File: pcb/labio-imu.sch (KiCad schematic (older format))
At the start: 33 parts, among them SW501 DIP_SWITCH_X04, U501 LSM303D, U502 BMP280, U503 L3GD20H

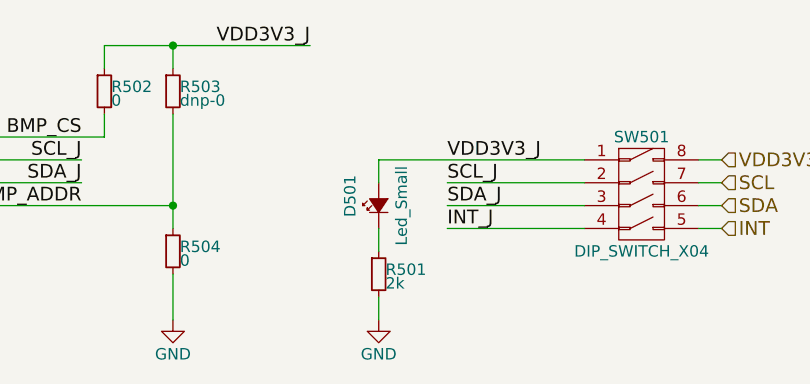
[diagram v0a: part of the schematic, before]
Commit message: add bom. change led resistors to 220 and dnp rpi hat eeprom
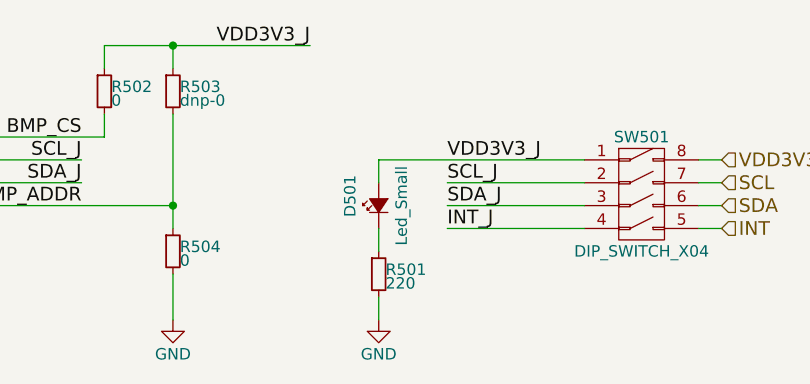
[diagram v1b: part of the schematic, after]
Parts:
- R501: value 2k -> 220
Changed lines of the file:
@@
 P 5000 7200
 F 0 "R501" H 5030 7220 50  0000 L CNN
-F 1 "2k" H 5030 7160 50  0000 L CNN
+F 1 "220" H 5030 7160 50  0000 L CNN
 F 2 "Resistors_SMD:R_0603" H 5000 7200 50  0001 C CNN
 F 3 "" H 5000 7200 50  0000 C CNN

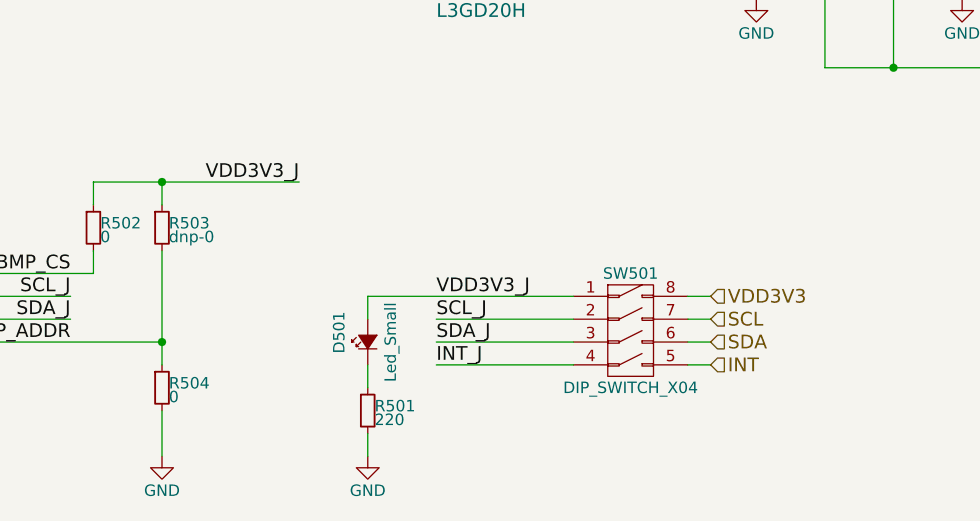
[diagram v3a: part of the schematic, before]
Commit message: Fix ADC reading mic, possible backpowering, encoder pull downs, vias in footprint:
* Mic needs on-board path to ADC. Add proper bias and amp. Connect to ADC or codec with switches.
* Mic footprint (U701) flipped. Redraw footprint and adjust routing.
* Remove power from dip switches and replace with fuses. Turning power off to a block could result in backpower from driven IO lines.
* Remove/adjust pull downs on LEDs for encoder/dpad lines.
* Move vias out of display connector (P401) footprint.
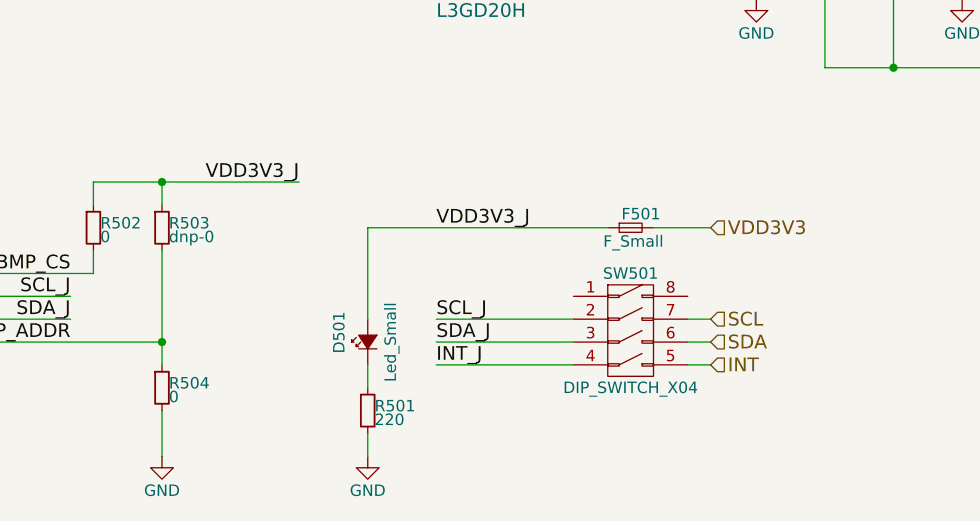
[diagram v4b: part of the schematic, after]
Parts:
- added F501: F_Small, Resistors_SMD:R_1206, symbol F_Small
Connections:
- net VDD3V3: now also F501.2; no longer SW501.8 (1B)
- net VDD3V3_J: now also F501.1; no longer SW501.1 (1A)
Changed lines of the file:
@@
 encoding utf-8
 Sheet 5 10
-Title ""
+Title "Raspberry Pi Embedded Lab I/O"
 Date ""
-Rev ""
-Comp ""
+Rev "1.1.4"
+Comp "Carnegie Mellon University"
 Comment1 ""
-Comment2 ""
+Comment2 "Drawn by: Ian Hartwig"
 Comment3 ""
 Comment4 ""
@@
 Text HLabel 6500 6900 2    60   Input ~ 0
 SDA
-Text HLabel 6500 6700 2    60   Input ~ 0
+Text HLabel 6500 6400 2    60   Input ~ 0
 VDD3V3
 Wire Wire Line
@@
 	1    0    0    -1
 $EndComp
-Wire Wire Line
-	6500 6700 6400 6700
 Wire Wire Line
 	6400 6800 6500 6800
@@
 $EndComp
 Wire Wire Line
-	5000 6700 5900 6700
-Wire Wire Line
 	5300 6800 5900 6800
 Wire Wire Line
@@
 Wire Wire Line
 	5300 7000 5900 7000
-Text Label 5300 6700 0    60   ~ 0
+Text Label 5300 6400 0    60   ~ 0
 VDD3V3_J
 Text Label 5300 6800 0    60   ~ 0
@@
 	5000 7400 5000 7300
 Wire Wire Line
-	5000 6700 5000 6800
+	5000 6400 5000 6800
 $Comp
 L GND #PWR015
@@
 	4100 7400 4100 7200
 Wire Wire Line
-	4100 7000 4100 6500
+	4100 6500 4100 7000
 Wire Wire Line
 	4100 6900 3300 6900
@@
 Text Label 4700 6200 2    60   ~ 0
 VDD3V3_J
+$Comp
+L F_Small F501
+U 1 1 57AFA57A
+P 6150 6400
+F 0 "F501" H 6110 6460 50  0000 L CNN
+F 1 "F_Small" H 6030 6340 50  0000 L CNN
+F 2 "Resistors_SMD:R_1206" H 6150 6400 50  0001 C CNN
+F 3 "" H 6150 6400 50  0000 C CNN
+	1    6150 6400
+	1    0    0    -1
+$EndComp
+Wire Wire Line
+	6250 6400 6500 6400
+Wire Wire Line
+	6050 6400 5000 6400
 $EndSCHEMATC

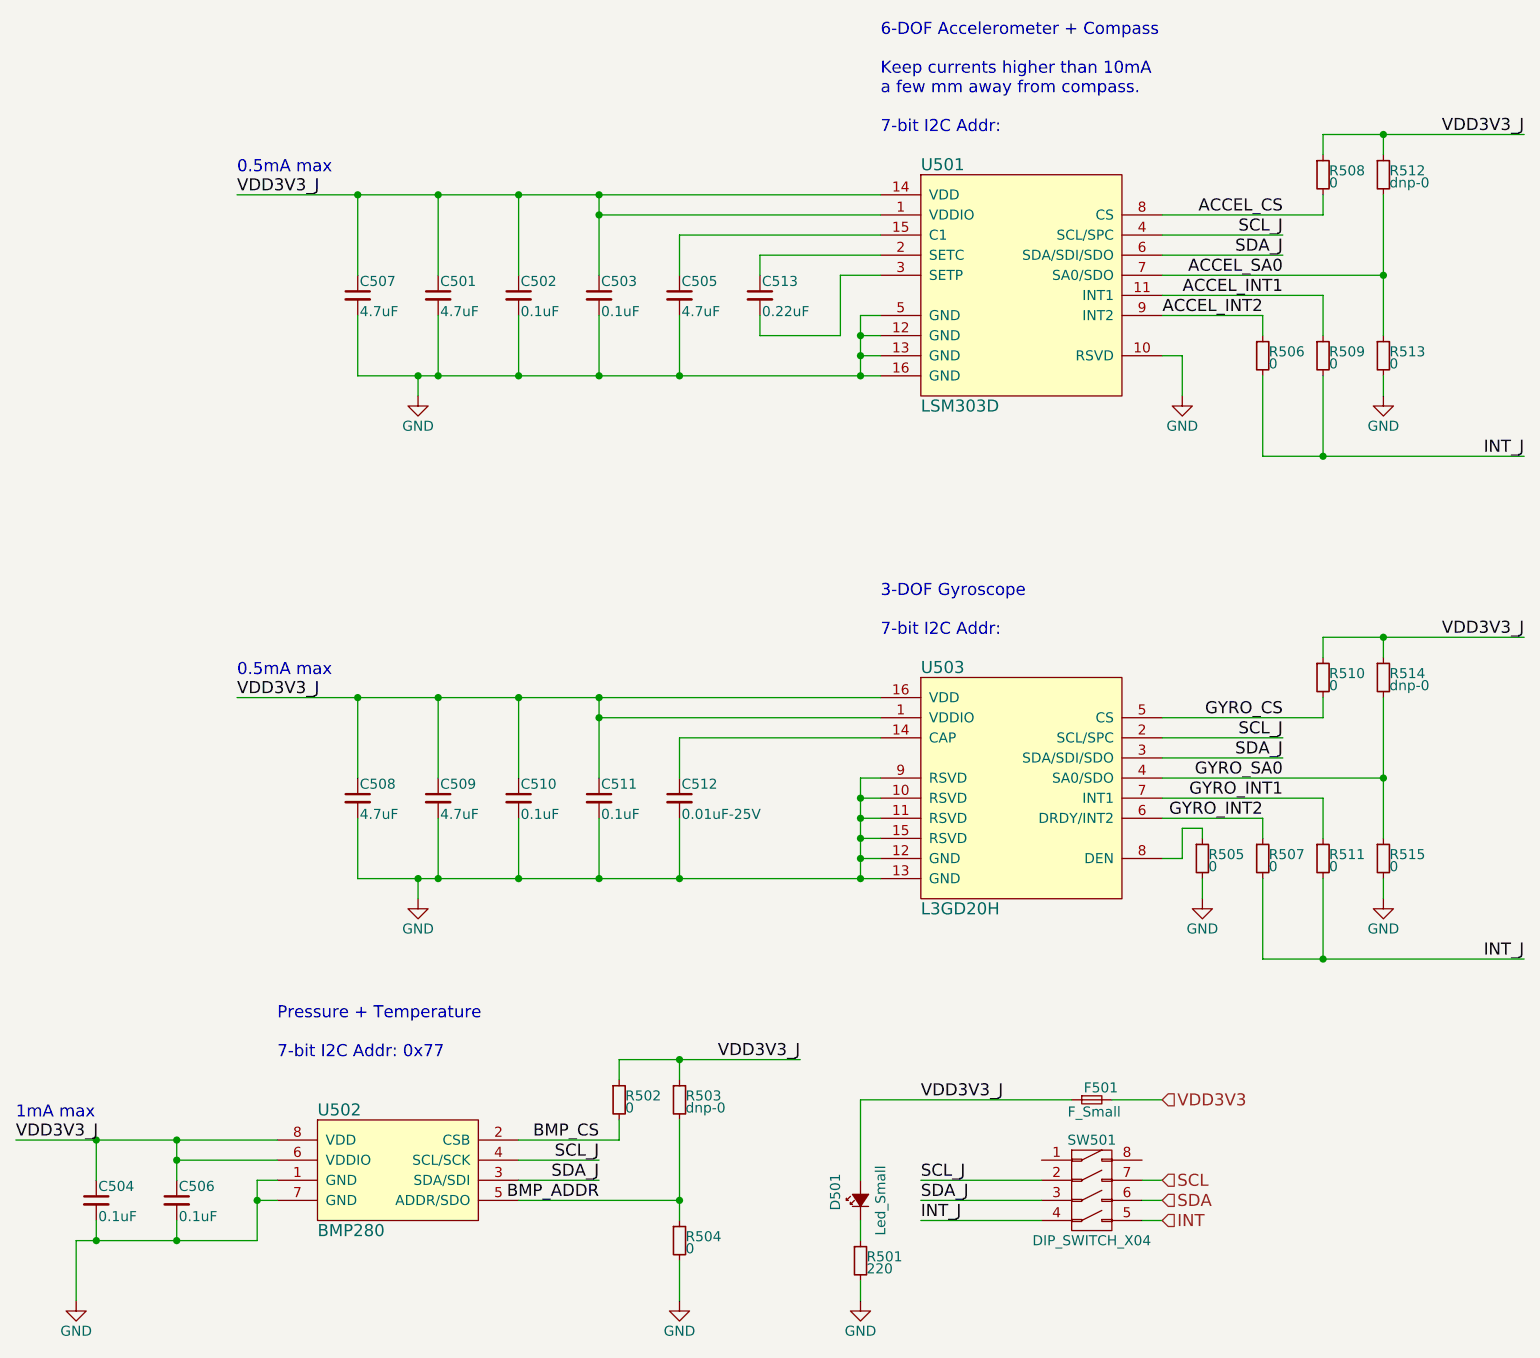
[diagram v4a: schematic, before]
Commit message: Fix i2c addresses, pressure sensor footprint, consolidate BOM
* Schematic should list I2C addresses for accelerometer, gyro.
* Pressure sensor footprint (U502) has pins in the wrong order. Redraw footprint and adjust routing.
* Bump i2c and photodiode pullups to 2.2k
* Remove R505 near gyro
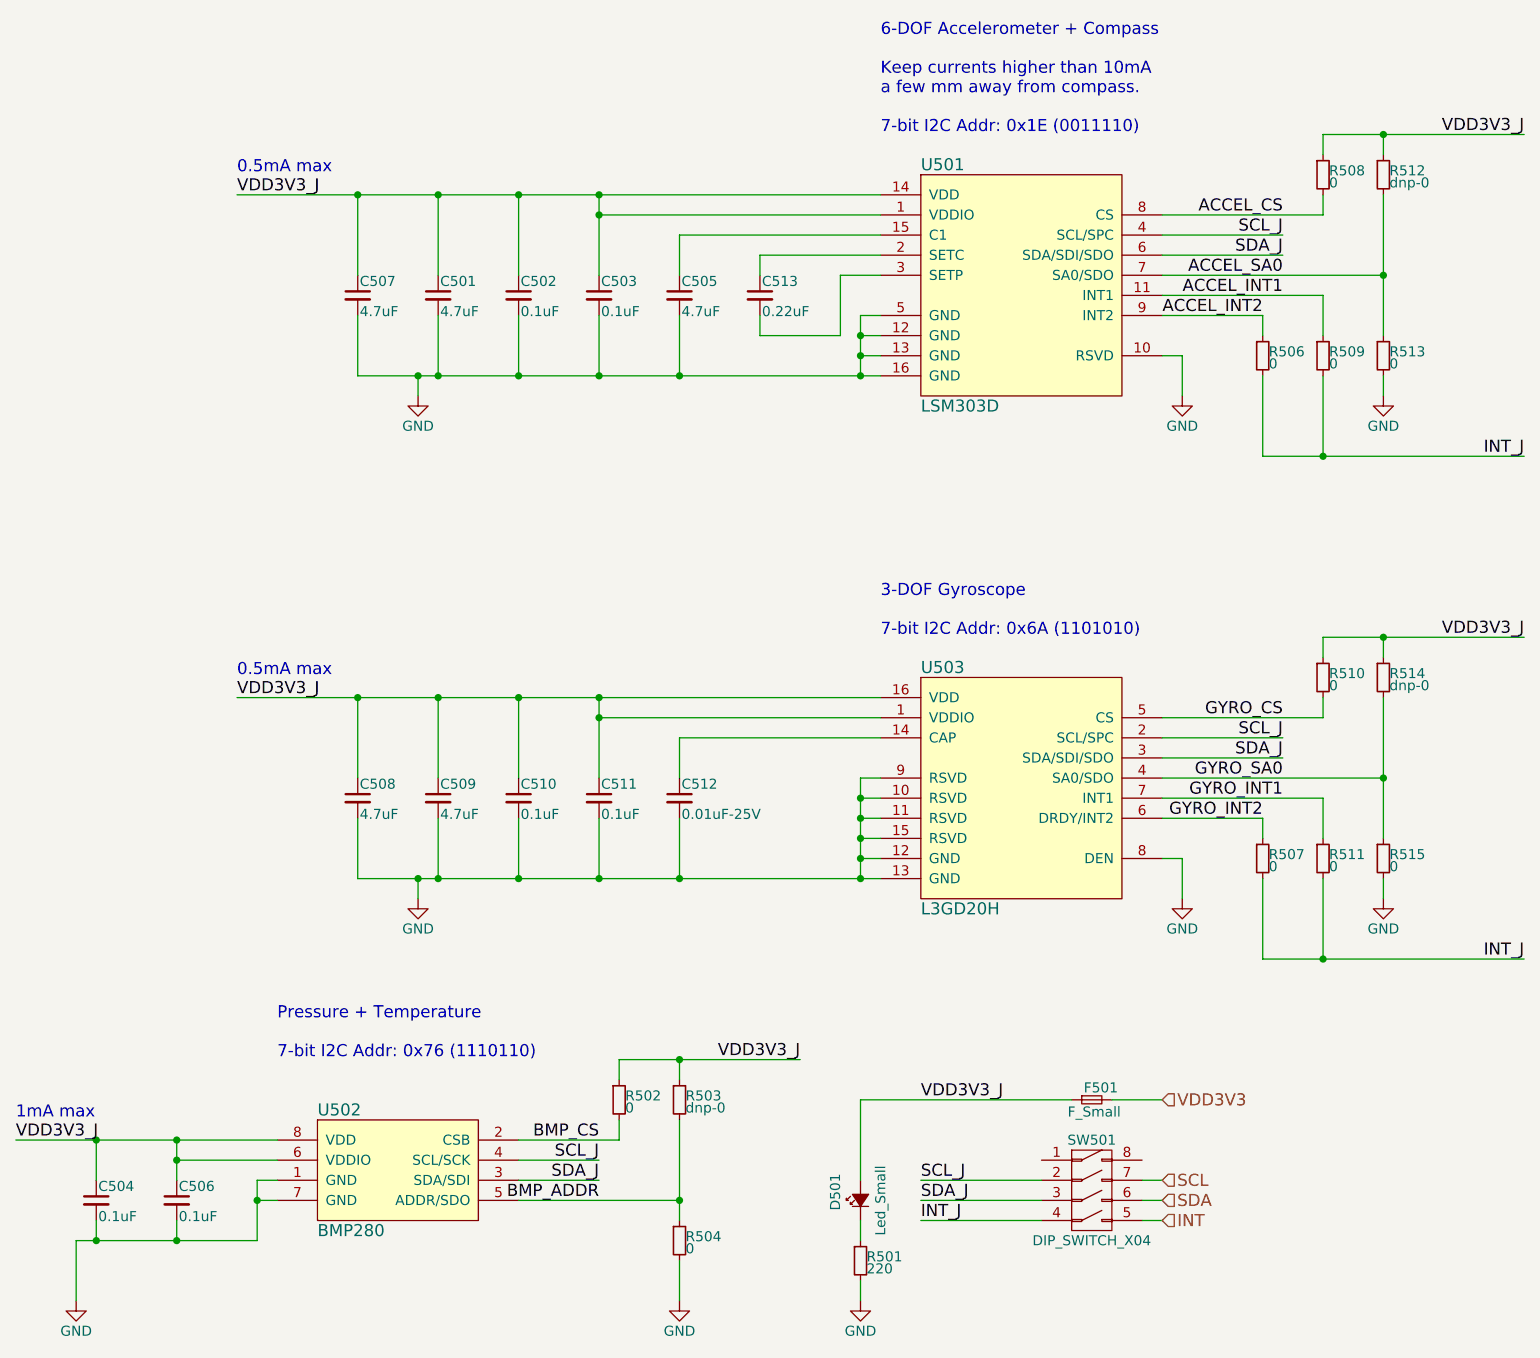
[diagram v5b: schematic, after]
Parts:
- removed R505: 0, Resistors_SMD:R_0603, symbol R_Small
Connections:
- net GND: now also U503.8 (DEN)
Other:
- note added: "3-DOF Gyroscope\n\n7-bit I2C Addr: 0x6A (1101010)"
- note added: "6-DOF Accelerometer + Compass\n\nKeep currents higher than 10mA\na few mm away from compass.\n\n7-bit I2C Addr: 0x1E (0011110)"
- note added: "Pressure + Temperature\n\n7-bit I2C Addr: 0x76 (1110110)"
- note removed: "3-DOF Gyroscope\n\n7-bit I2C Addr:"
- note removed: "6-DOF Accelerometer + Compass\n\nKeep currents higher than 10mA\na few mm away from compass.\n\n7-bit I2C Addr:"
- note removed: "Pressure + Temperature\n\n7-bit I2C Addr: 0x77"
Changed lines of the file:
@@
 $EndDescr
 Text Notes 5100 1600 0    60   ~ 0
-6-DOF Accelerometer + Compass\n\nKeep currents higher than 10mA\na few mm away from compass.\n\n7-bit I2C Addr:
+6-DOF Accelerometer + Compass\n\nKeep currents higher than 10mA\na few mm away from compass.\n\n7-bit I2C Addr: 0x1E (0011110)
 $Comp
 L GND #PWR010
@@
 $EndComp
 Text Notes 2100 6200 0    60   ~ 0
-Pressure + Temperature\n\n7-bit I2C Addr: 0x77
+Pressure + Temperature\n\n7-bit I2C Addr: 0x76 (1110110)
 Text Notes 1900 1800 0    60   ~ 0
 0.5mA max
@@
 	1    0    0    -1
 $EndComp
-$Comp
-L R_Small R505
-U 1 1 578C603B
-P 6700 5200
-F 0 "R505" H 6730 5220 50  0000 L CNN
-F 1 "0" H 6730 5160 50  0000 L CNN
-F 2 "Resistors_SMD:R_0603" H 6700 5200 50  0001 C CNN
-F 3 "" H 6700 5200 50  0000 C CNN
-	1    6700 5200
-	1    0    0    -1
-$EndComp
-Wire Wire Line
-	6700 5100 6700 5050
-Wire Wire Line
-	6700 5050 6600 5050
-Wire Wire Line
-	6600 5050 6600 5200
 Wire Wire Line
 	6600 5200 6500 5200
@@
 L GND #PWR017
 U 1 1 578C6171
-P 6700 5400
-F 0 "#PWR017" H 6700 5150 50  0001 C CNN
-F 1 "GND" H 6700 5250 50  0000 C CNN
-F 2 "" H 6700 5400 50  0000 C CNN
-F 3 "" H 6700 5400 50  0000 C CNN
-	1    6700 5400
-	1    0    0    -1
-$EndComp
-Wire Wire Line
-	6700 5400 6700 5300
+P 6600 5400
+F 0 "#PWR017" H 6600 5150 50  0001 C CNN
+F 1 "GND" H 6600 5250 50  0000 C CNN
+F 2 "" H 6600 5400 50  0000 C CNN
+F 3 "" H 6600 5400 50  0000 C CNN
+	1    6600 5400
+	1    0    0    -1
+$EndComp
 $Comp
 L C_Small C508
@@
 Connection ~ 2800 2800
 Text Notes 5100 4100 0    60   ~ 0
-3-DOF Gyroscope\n\n7-bit I2C Addr:
+3-DOF Gyroscope\n\n7-bit I2C Addr: 0x6A (1101010)
 Wire Wire Line
 	1100 7400 1100 7100
@@
 Wire Wire Line
 	6050 6400 5000 6400
+Wire Wire Line
+	6600 5400 6600 5200
 $EndSCHEMATC
